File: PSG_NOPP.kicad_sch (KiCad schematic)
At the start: 13 parts, among them CON1 AudioJack3_SwitchTR, U12 AY-3-8913, X3 2 MHz

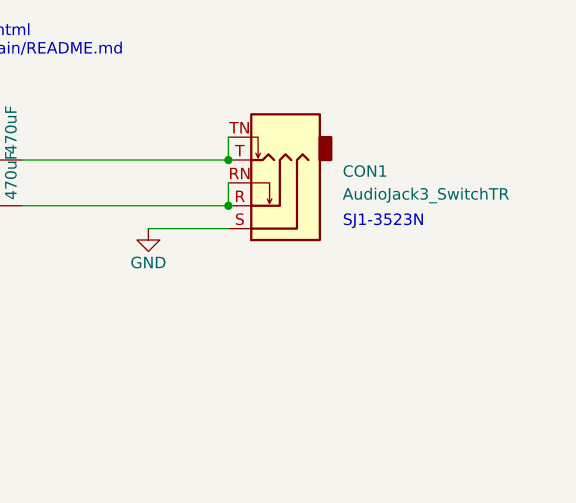
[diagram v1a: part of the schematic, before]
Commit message: Update part numbers.
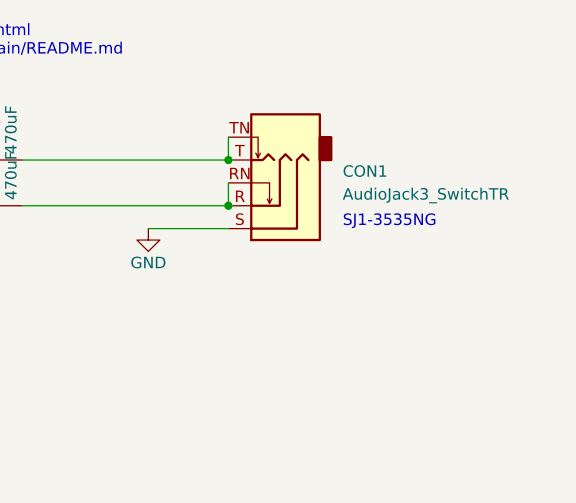
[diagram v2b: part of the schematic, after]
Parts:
- CON1: PartNum00 490-SJ1-3533NG -> 490-SJ1-3535NG
- U12: PartNum01 737-ICS-624-T -> 737-ICM-624-1-GT-HT
- X3: PartNum00 520-TCH200-X -> 774-MXO45HS2C2M0000
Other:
- note added: "SJ1-3535NG"
- note removed: "SJ1-3523N"
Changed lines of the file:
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@@
 		)
 	)
-	(text "SJ1-3523N"
+	(text "SJ1-3535NG"
 		(exclude_from_sim no)
 		(at 213.36 41.91 0)
@@
 			)
 		)
-		(property "PartNum01" "737-ICS-624-T"
+		(property "PartNum01" "737-ICM-624-1-GT-HT"
 			(at 91.44 93.98 0)
 			(effects
@@
 			)
 		)
-		(property "PartNum00" "520-TCH200-X"
+		(property "PartNum00" "774-MXO45HS2C2M0000"
 			(at 22.86 120.65 0)
 			(effects
@@
 			)
 		)
-		(property "PartNum00" "490-SJ1-3533NG"
+		(property "PartNum00" "490-SJ1-3535NG"
 			(at 205.74 39.37 0)
 			(effects
